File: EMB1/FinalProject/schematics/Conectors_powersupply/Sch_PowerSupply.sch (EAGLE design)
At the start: 11 parts, among them IC2 LM2574N-3.3, K1 61201021621

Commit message: changes in pcb
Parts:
- removed K1: 61201021621, Wurth_Elektronik_Electromechanic_Wire_to_Board_Connectors_rev15c:61201021621
- added ENCODER1, ENCODER2: (no value), con-amp-quick:M03
- added SL2: (no value), con-amp-quick:M02
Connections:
- removed net LBACK+: FPGA11/20.2, K1.5
- removed net LBACK-: FPGA11/20.1, K1.3
- removed net LFWD+: FPGA11/20.3, K1.7
- removed net LFWD-: FPGA1/10.10, K1.1
- removed net RBACK+: FPGA11/20.5, K1.6
- removed net RBACK-: FPGA11/20.6, K1.4
- removed net RFWD+: FPGA11/20.4, K1.8
- removed net RFWD-: FPGA11/20.7, K1.2
- new net N$11: FPGA1/10.9
- new net N$12: FPGA1/10.8
- new net N$7: FPGA11/20.3
- new net N$8: FPGA11/20.2
- new net SIGNAL1: ENCODER1.3, FPGA1/10.6
- new net SIGNAL2: ENCODER2.3, FPGA1/10.7
- net 3.3V: now also ENCODER1.1, ENCODER2.1
- net 5V: now also SL2.2
- net CL: now also FPGA11/20.4; no longer FPGA1/10.6
- net GND: now also ENCODER1.2, ENCODER2.2, SL2.1
- net MISO: now also FPGA11/20.5; no longer FPGA1/10.7
- net MOSI: now also FPGA11/20.7; no longer FPGA1/10.9
- net N$10: now also FPGA1/10.10; no longer K1.10
- net N$9: now also FPGA11/20.1; no longer K1.9
- net SCL: now also FPGA11/20.6; no longer FPGA1/10.8

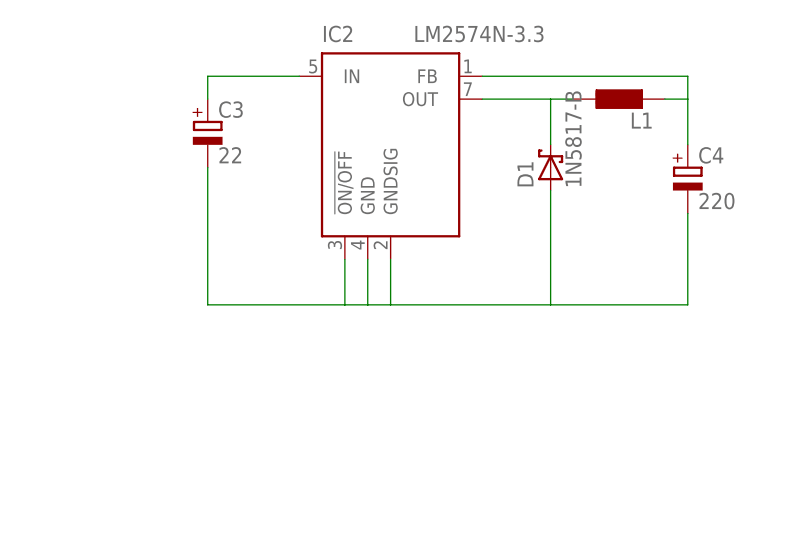
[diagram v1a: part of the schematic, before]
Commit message: Powersupply section added
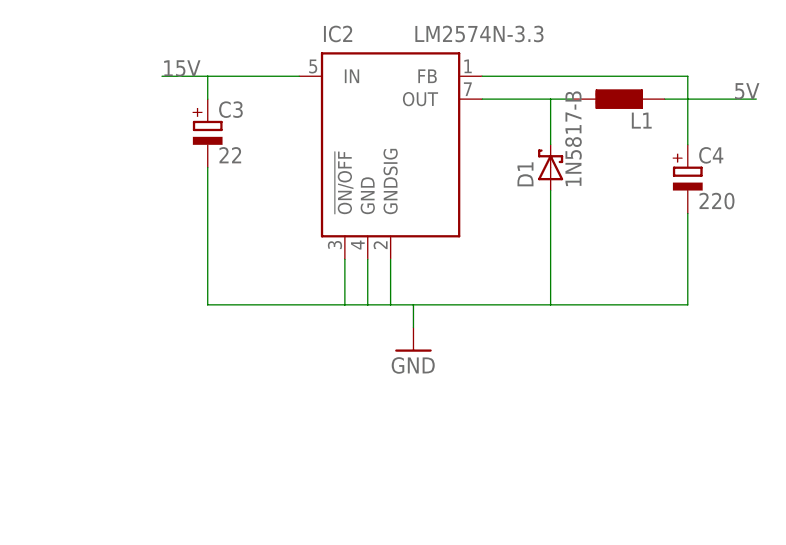
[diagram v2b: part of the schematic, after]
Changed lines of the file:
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@@
 <part name="ENCODER2" library="con-amp-quick" deviceset="M03" device=""/>
 <part name="SL2" library="con-amp-quick" deviceset="M02" device=""/>
+<part name="GND1" library="supply1" deviceset="GND" device=""/>
 </parts>
 <sheets>
@@
 <instance part="ENCODER2" gate="G$1" x="20.32" y="12.7"/>
 <instance part="SL2" gate="G$1" x="25.4" y="88.9"/>
+<instance part="GND1" gate="1" x="142.24" y="81.28"/>
 </instances>
 <busses>
@@
 <wire x1="172.72" y1="86.36" x2="157.48" y2="86.36" width="0.1524" layer="91"/>
 <pinref part="D1" gate="G$1" pin="A"/>
-<wire x1="157.48" y1="86.36" x2="139.7" y2="86.36" width="0.1524" layer="91"/>
+<wire x1="157.48" y1="86.36" x2="142.24" y2="86.36" width="0.1524" layer="91"/>
+<wire x1="142.24" y1="86.36" x2="139.7" y2="86.36" width="0.1524" layer="91"/>
 <wire x1="157.48" y1="99.06" x2="157.48" y2="86.36" width="0.1524" layer="91"/>
 <pinref part="C3" gate="G$1" pin="-"/>
 <wire x1="119.38" y1="101.6" x2="119.38" y2="86.36" width="0.1524" layer="91"/>
 <wire x1="119.38" y1="86.36" x2="134.62" y2="86.36" width="0.1524" layer="91"/>
+<pinref part="GND1" gate="1" pin="GND"/>
+<wire x1="142.24" y1="83.82" x2="142.24" y2="86.36" width="0.1524" layer="91"/>
 </segment>
 <segment>
@@
 <wire x1="119.38" y1="109.22" x2="119.38" y2="111.76" width="0.1524" layer="91"/>
 <wire x1="119.38" y1="111.76" x2="129.54" y2="111.76" width="0.1524" layer="91"/>
+<wire x1="119.38" y1="111.76" x2="114.3" y2="111.76" width="0.1524" layer="91"/>
+<label x="114.3" y="111.76" size="1.778" layer="95"/>
 </segment>
 </net>
@@
 <wire x1="149.86" y1="111.76" x2="172.72" y2="111.76" width="0.1524" layer="91"/>
 <wire x1="172.72" y1="111.76" x2="172.72" y2="109.22" width="0.1524" layer="91"/>
+<wire x1="172.72" y1="109.22" x2="180.34" y2="109.22" width="0.1524" layer="91"/>
+<label x="177.8" y="109.22" size="1.778" layer="95"/>
 </segment>
 <segment>
